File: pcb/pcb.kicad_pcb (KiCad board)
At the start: 2 copper layers, 276.2 x 78.9 mm, 127 parts, among them J1 USB_C_Receptacle_USB2.0, J2 AVR-ISP-6, SW1 SW_Push, U1 ATmega32U4-AU, U2 PRTR5V0U2X, Y1 16MHz

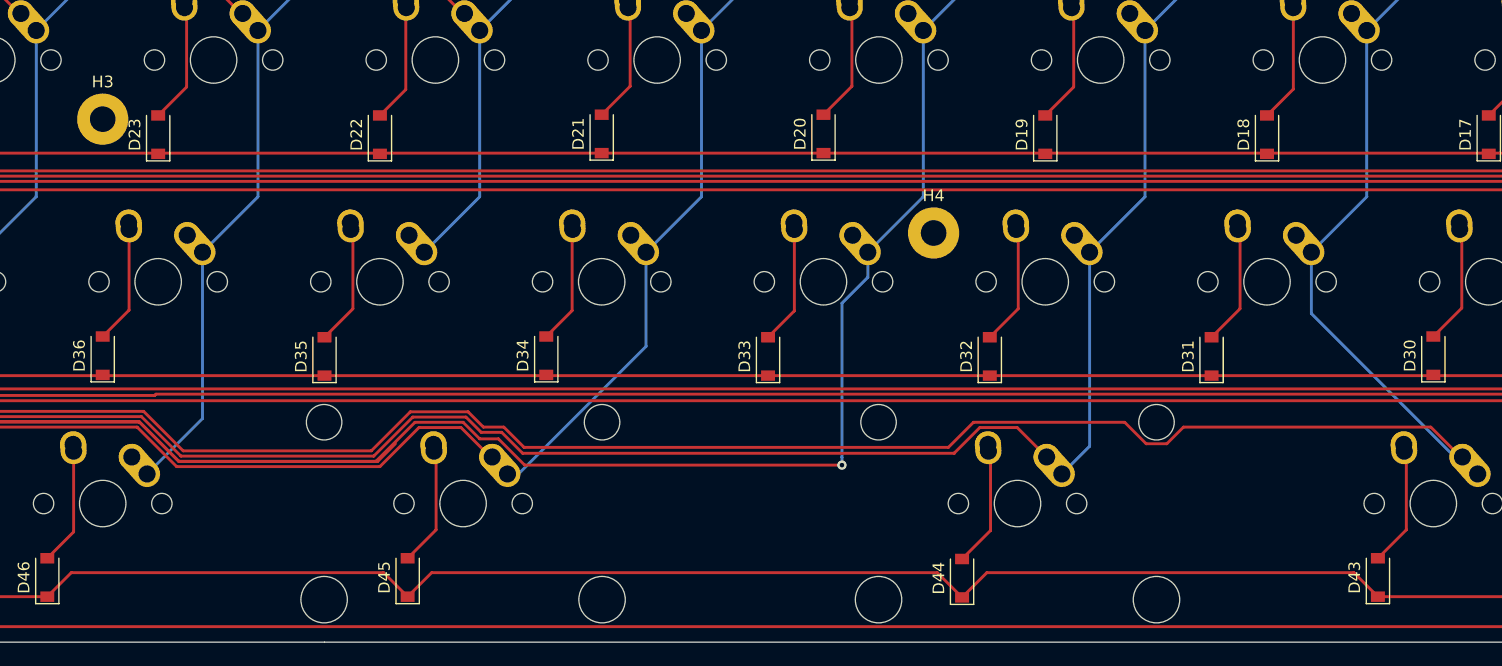
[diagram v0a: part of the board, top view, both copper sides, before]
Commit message: correct spacebar placements
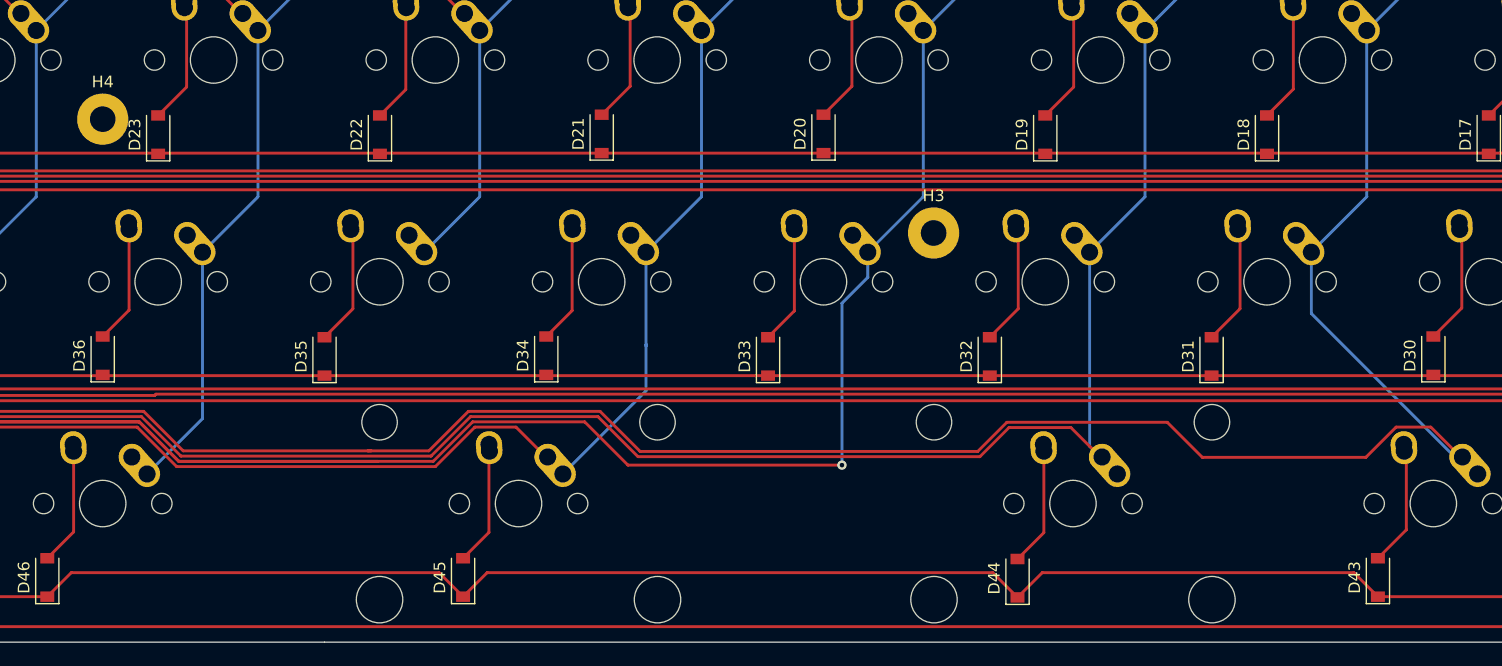
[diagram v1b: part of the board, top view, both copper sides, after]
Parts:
- removed the H3 at (165.1, 113.0)
- added H4: MountingHole, MountingHole:MountingHole_2.2mm_M2_Pad, F.Cu at (165.1, 113.0)
- H1, H2, H5, H6: value MountingHole_2.2mm_M2_Pad -> MountingHole
- H3: renamed from H4; value MountingHole_2.2mm_M2_Pad -> MountingHole
- MX44: footprint MX_Alps_Hybrid:MX-2.75U-NoLED -> MX_Alps_Hybrid:MX-2.25U-NoLED
- MX45: footprint MX_Alps_Hybrid:MX-2.25U-NoLED -> MX_Alps_Hybrid:MX-2.75U-NoLED
- moved D44 4.76 mm to (243.7, 152.5)
- moved D45 4.76 mm to (196.1, 152.4)
- moved MX44 4.76 mm to (248.4, 146.1)
- moved MX45 4.76 mm to (200.8, 146.1)
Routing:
- net COL4: track 236.1 -> 243.1 mm
- net COL6: track 194.5 -> 196.9 mm
- net COL5: track 268.2 -> 266.1 mm
- net Net-(D45-Pad2): track 10.3 -> 12.3 mm
- net COL3: track 279.4 -> 281.0 mm

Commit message: flip stabs on space
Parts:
- MX44: footprint MX_Alps_Hybrid:MX-2.25U-NoLED -> MX_Alps_Hybrid:MX-2.25U-ReversedStabilizers-NoLED
- MX45: footprint MX_Alps_Hybrid:MX-2.75U-NoLED -> MX_Alps_Hybrid:MX-2.75U-ReversedStabilizers-NoLED
- moved D31 3.18 mm to (257.2, 133.4)
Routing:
- net COL1: track 309.6 -> 343.0 mm
- net COL2: track 289.1 -> 296.8 mm
- net COL0: track 318.8 -> 326.5 mm
- net ROW3: track 301.5 -> 304.5 mm
- net Net-(D31-Pad2): track 10.9 -> 12.9 mm
- net COL3: track 281.0 -> 281.8 mm

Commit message: 3mm outer spacing
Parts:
- moved C1 11.1 mm to (112.7, 121.1)
- moved C2 11.1 mm to (101.0, 130.3)
- moved C3 11.1 mm to (100.8, 137.4)
- moved C4 11.1 mm to (100.8, 141.0)
- moved C5 11.1 mm to (100.8, 133.9)
- moved C7 11.1 mm to (103.1, 106.9)
- moved D11 11.1 mm to (152.4, 96.1)
- moved D13 11.1 mm to (112.7, 96.0)
- moved D15 11.1 mm to (338.1, 115.2)
- moved D16 11.1 mm to (314.3, 115.1)
- moved D18 11.1 mm to (276.2, 115.2)
- moved D19 11.1 mm to (257.2, 115.2)
- moved D2 11.1 mm to (323.9, 96.1)
- moved D20 11.1 mm to (238.1, 115.1)
- moved D22 11.1 mm to (200.0, 115.2)
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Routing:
- net ROW2: track 581.8 -> 581.2 mm
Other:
- board size 276.2 x 78.9 mm -> 277 x 77.4 mm

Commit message: center isp and reroute tracks
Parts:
- moved Y1 11.3 mm to (100.8, 106.7)
- moved C6 8.70 mm to (108.2, 104.0), turned to 0 degrees
- moved U2 8.59 mm to (334.2, 107.4), turned to 270 degrees
- moved R4 6.42 mm to (108.2, 100.8), turned to 0 degrees
- moved C7 5.15 mm to (108.2, 107.0), turned to 0 degrees
- moved R3 4.14 mm to (328.5, 105.6), turned to 0 degrees
- moved C1 3.87 mm to (115.9, 118.9)
- moved F1 3.59 mm to (334.2, 112.5), turned to 90 degrees
- moved SW1 3.19 mm to (100.8, 100.7), turned to 90 degrees
- moved J2 2.83 mm to (90.6, 122.5)
- moved R5 2.74 mm to (336.6, 100.9)
- moved R6 2.08 mm to (331.8, 100.9)
- moved U1 1.73 mm to (104.8, 120.7)
- moved R1 0.79 mm to (101.7, 144.0)
- moved C2 0.79 mm to (101.8, 130.3)
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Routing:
- net GND: track 358.0 -> 445.7 mm, vias 4 -> 6
- net +5V: track 274.3 -> 361.4 mm, vias 3 -> 8
- net COL5: track 266.1 -> 215.7 mm
- net COL0: track 326.5 -> 297.9 mm
- net COL1: track 343.0 -> 319.4 mm
- net VCC: track 24.8 -> 38.8 mm, vias 0 -> 2
- net ROW2: track 581.2 -> 571.2 mm
- net ROW0: track 270.6 -> 261.9 mm
- net Net-(C7-Pad1): track 20.9 -> 13.9 mm, vias 2 -> 0
- net ROW3: track 304.5 -> 298.5 mm
- net D+: track 233.8 -> 229.7 mm
- net COL6: track 196.8 -> 193.4 mm
- net Net-(J1-PadA7): track 34.5 -> 37.9 mm, vias 2 -> 4
- net RST: track 55.5 -> 52.3 mm
- net COL8: track 159.8 -> 162.6 mm, vias 0 -> 1
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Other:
- board size 277 x 77.4 mm -> 277 x 77.6 mm

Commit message: add LED and reshape width of macros spacer
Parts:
- added D51: WS2812B, LED_SMD:LED_WS2812B_PLCC4_5.0x5.0mm_P3.2mm, B.Cu at (81.3, 127.0)
- added MX51: MX-NoLED, MX_Alps_Hybrid:MX-1.25U-NoLED, B.Cu at (331.3, 145.9)
- added MX52: MX-NoLED, MX_Alps_Hybrid:MX-1.25U-NoLED, B.Cu at (307.5, 145.9)
- added MX53: MX-NoLED, MX_Alps_Hybrid:MX-1.25U-NoLED, B.Cu at (283.7, 145.9)
- added MX54: MX-NoLED, MX_Alps_Hybrid:MX-6U-Centered-ReversedStabilizers-NoLED, B.Cu at (214.6, 145.9)
- added R7: 330, Resistor_SMD:R_0805_2012Metric, F.Cu at (80.2, 133.0)
- E1: moved to F.Cu
- moved R1 21.5 mm to (83.3, 133.0), turned to 90 degrees
- moved D40 19.3 mm to (323.9, 150.1)
- moved H4 19.2 mm to (157.5, 117.9)
- moved H2 18.9 mm to (324.1, 138.7)
- moved C4 16.4 mm to (87.8, 132.1)
- moved R5 16.0 mm to (320.5, 100.5)
- moved H6 15.5 mm to (90.9, 138.7)
- moved D28 15.1 mm to (321.0, 130.9)
- moved D18 15.1 mm to (261.5, 111.9)
- moved D2 15.1 mm to (309.1, 92.8)
- moved D3 15.1 mm to (290.1, 92.8)
- moved D38 15.1 mm to (123.4, 130.9)
- moved D32 15.1 mm to (237.7, 130.9)
- moved D33 15.1 mm to (218.6, 130.9)
- moved D34 15.1 mm to (199.6, 130.8)
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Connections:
- U1 pad 18: ROW1 -> ROW0
- U1 pad 19: ROW0 -> ROW1
- U1 pad 20: Net-(U1-Pad20) -> COL12
- U1 pad 25: SCK -> MISO
- U1 pad 27: MISO -> SCK
- U1 pad 32: COL12 -> LED
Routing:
- net VCC: track 38.8 -> 291.7 mm, vias 2 -> 3
- net Net-(D45-Pad2): track 10.1 -> 37.8 mm
- net COL12: track 82.0 -> 108.9 mm, vias 0 -> 1
- net COL0: track 297.9 -> 322.4 mm, vias 0 -> 1
- net Net-(D51-Pad4): track 0.00 -> 15.4 mm, vias 0 -> 1
- net COL4: track 244.3 -> 229.1 mm
- net LED: track 0.00 -> 14.9 mm
- net COL3: track 280.9 -> 266.2 mm
- net COL6: track 193.4 -> 207.5 mm
- net Net-(D40-Pad2): track 10.7 -> 23.0 mm
- net COL7: track 160.9 -> 151.4 mm, vias 1 -> 0
- net COL8: track 162.6 -> 153.4 mm, vias 1 -> 0
- net COL9: track 143.7 -> 135.0 mm, vias 1 -> 0
- net COL10: track 124.7 -> 116.0 mm, vias 1 -> 0
- net Net-(R1-Pad2): track 20.1 -> 12.2 mm
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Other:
- board size 277 x 77.6 mm -> 272.3 x 77.6 mm

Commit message: gnd zone fill
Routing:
- added copper zone on B.Cu, net GND
- added copper zone on F.Cu, net GND
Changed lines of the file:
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@@
   (segment (start 80.16875 128.61925) (end 80.16875 132.55625) (width 0.25) (layer F.Cu) (net 94))
   (segment (start 86.230729 122.557271) (end 80.16875 128.61925) (width 0.25) (layer F.Cu) (net 94))
+  (zone (net 1) (net_name GND) (layer B.Cu) (hatch edge 0.508)
+    (connect_pads (clearance 0.508))
+    (min_thickness 0.254)
+    (fill yes (arc_segments 32) (thermal_gap 0.508) (thermal_bridge_width 0.508))
+    (polygon
+      (pts
+        (xy 345.44 157.48) (xy 70.612 157.988) (xy 70.612 76.2) (xy 345.44 76.2)
+      )
+    )
+  )
+  (zone (net 1) (net_name GND) (layer F.Cu) (hatch edge 0.508)
+    (connect_pads (clearance 0.508))
+    (min_thickness 0.254)
+    (fill yes (arc_segments 32) (thermal_gap 0.508) (thermal_bridge_width 0.508))
+    (polygon
+      (pts
+        (xy 345.44 157.48) (xy 70.612 157.988) (xy 70.612 76.2) (xy 345.44 76.2)
+      )
+    )
+  )
 )

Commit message: add silkscreen design to pcb
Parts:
- added G1: LOGO, graphics:logo.pretty, F.Cu at (311.8, 117.5)
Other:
- board text added: "Inaba40 rev1.0"

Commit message: move mounting holes and flip silk screen on pcb
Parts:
- moved H5 1.27 mm to (92.2, 95.5)
- moved H6 1.27 mm to (92.2, 138.7)
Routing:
- net +5V: track 361.3 -> 360.5 mm
- net GND: track 450.3 -> 449.8 mm
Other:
- board text added: "Designed by MayTD"
